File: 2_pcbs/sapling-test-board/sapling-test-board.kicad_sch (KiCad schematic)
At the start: 24 parts, among them IC1 LED driver TLC59281DBQR, IC2 LED driver TLC59281DBQR, IC3 74HC138D, J1 Pin header BCS-112-L-D-PE, J2 UJC-HP-3-SMT-TR

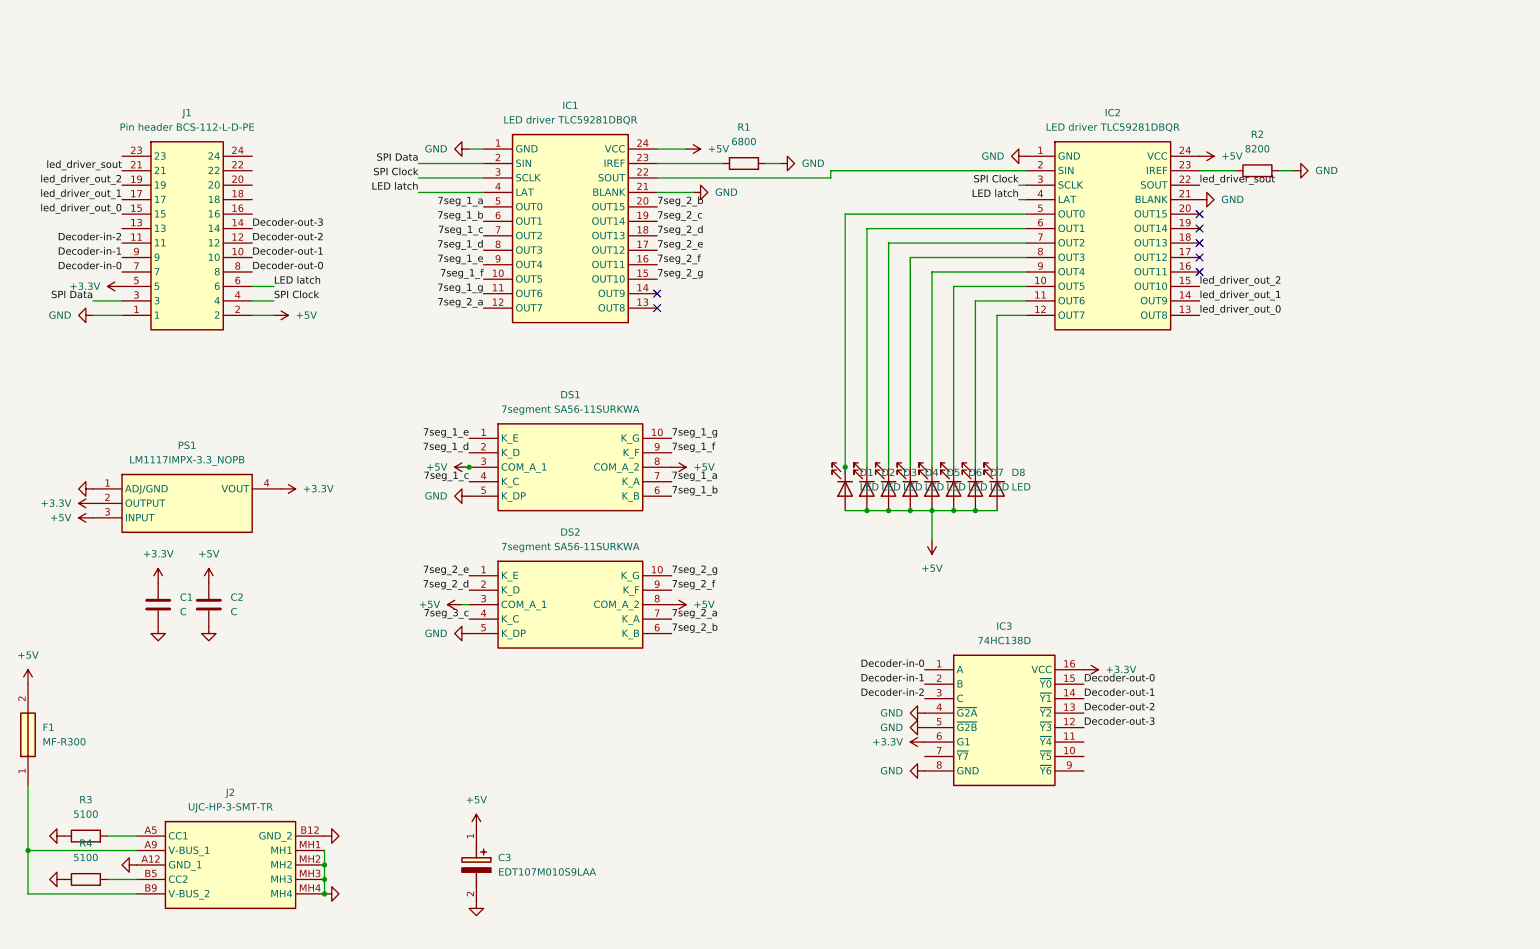
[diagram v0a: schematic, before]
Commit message: Hand routed PCB
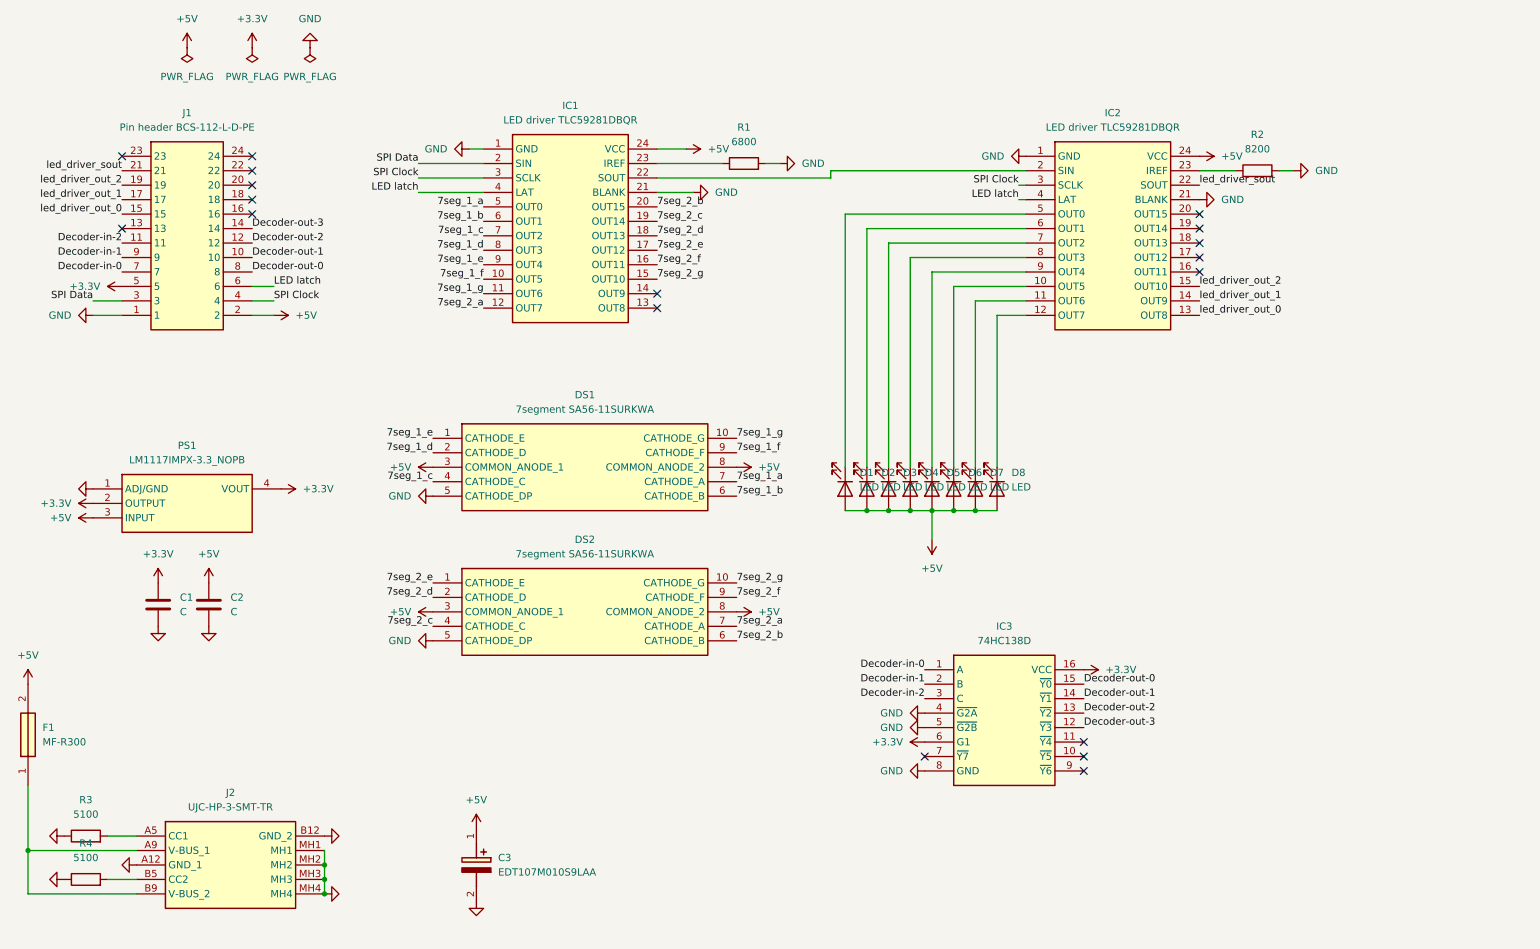
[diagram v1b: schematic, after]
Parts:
- C1, C2: footprint (none) -> Capacitor_SMD:C_0805_2012Metric
- C3: footprint CAPAE830X650N -> 100uf 10v Electrolytic cap:CAPAE830X650N
- D1, D2, D3, D4, D5, D6, D7, D8: footprint (none) -> LED_THT:LED_D5.0mm
- DS1, DS2: footprint DIPS1524W75P254L1270H825Q10N -> 7-segment:DIPS1524W75P254L1270H825Q10N; symbol 7-segment:SA56-11SURKWA -> 7-segment:SA56-11CGKWA; Manufacturer_Part_Number SA56-11SURKWA -> SA56-11CGKWA; Mouser Part Number 604-SA56-11SURKWA -> 604-SA56-11CGKWA; Mouser Price/Stock https://www.mouser.co.uk/ProductDetail/Kingbright/SA56-11SU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 -> https://www.mouser.co.uk/ProductDetail/Kingbright/SA56-11CG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
- F1: footprint MFR300 -> Resettable fuse:MFR300
- IC1, IC2: footprint SOP64P600X175-24N -> LED driver:SOP64P600X175-24N
- IC3: footprint SOIC127P600X175-16N -> 3-8 decoder:SOIC127P600X175-16N
- J1: footprint BCS-112-XXX-D-PE -> Pin header:BCS-112-XXX-D-PE
- J2: footprint UJCHP3SMTTR -> USB-C plug:UJCHP3SMTTR
- PS1: footprint SOT230P700X180-4N -> 3.3v regulator:SOT230P700X180-4N
- R1, R2, R3, R4: footprint (none) -> Resistor_SMD:R_0805_2012Metric
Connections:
- net 7seg_3_c is gone; now on net 7seg_2_c: DS2.4 (CATHODE_C)
- no-connect marks 7 -> 18
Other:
- moved on the sheet: DS1, DS2

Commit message: BB PCB review
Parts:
- added C4, C5, C6: 100nf, Capacitor_SMD:C_0805_2012Metric, symbol Device:C
- added TP1: LED Driver 2 sout, TestPoint:TestPoint_Pad_D4.0mm, symbol Connector:TestPoint
- added TP2: +5v, TestPoint:TestPoint_Pad_D4.0mm, symbol Connector:TestPoint
- added TP3: GND, TestPoint:TestPoint_Pad_D4.0mm, symbol Connector:TestPoint
- added TP4: +3.3v, TestPoint:TestPoint_Pad_D4.0mm, symbol Connector:TestPoint
- added TP5: SIN between, TestPoint:TestPoint_Pad_D4.0mm, symbol Connector:TestPoint
- C1, C2: value C -> 500nf
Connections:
- net +3.3V: now also C4.2, TP4.1
- net +5V: now also C5.2, C6.2, TP2.1
- net GND: now also C4.1, C5.1, C6.1, TP3.1
- net led_driver_sout: now also TP1.1
- net at IC1.22 (SOUT), IC2.2 (SIN): now also TP5.1

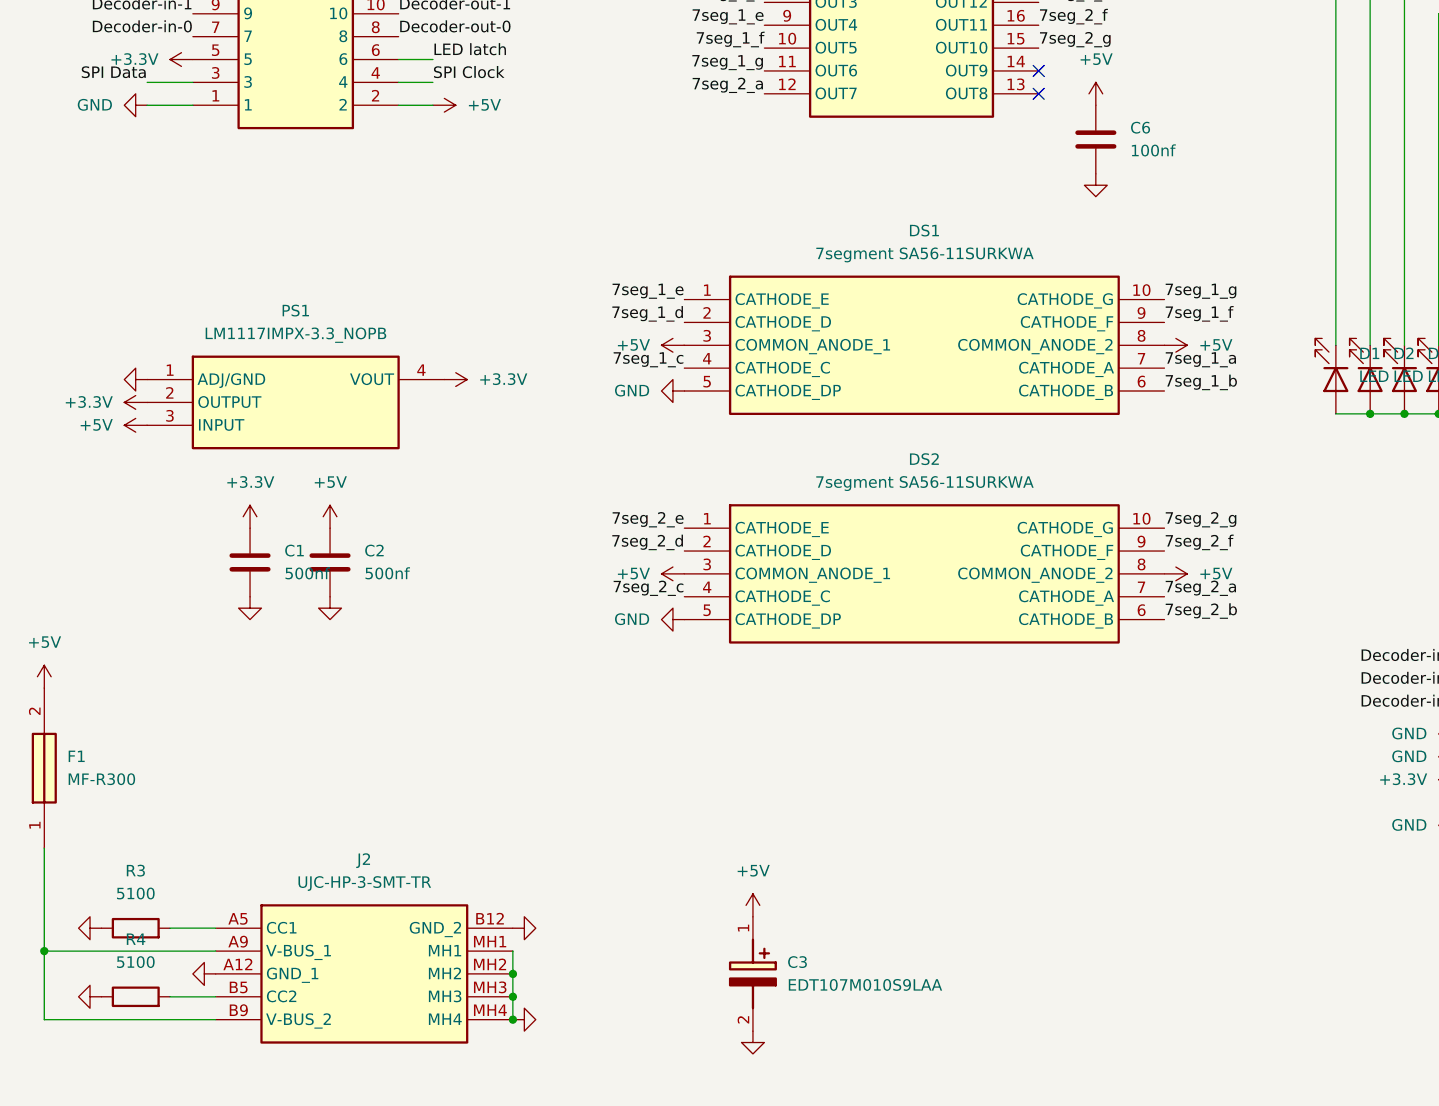
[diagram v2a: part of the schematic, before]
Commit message: Test board PCB ordered
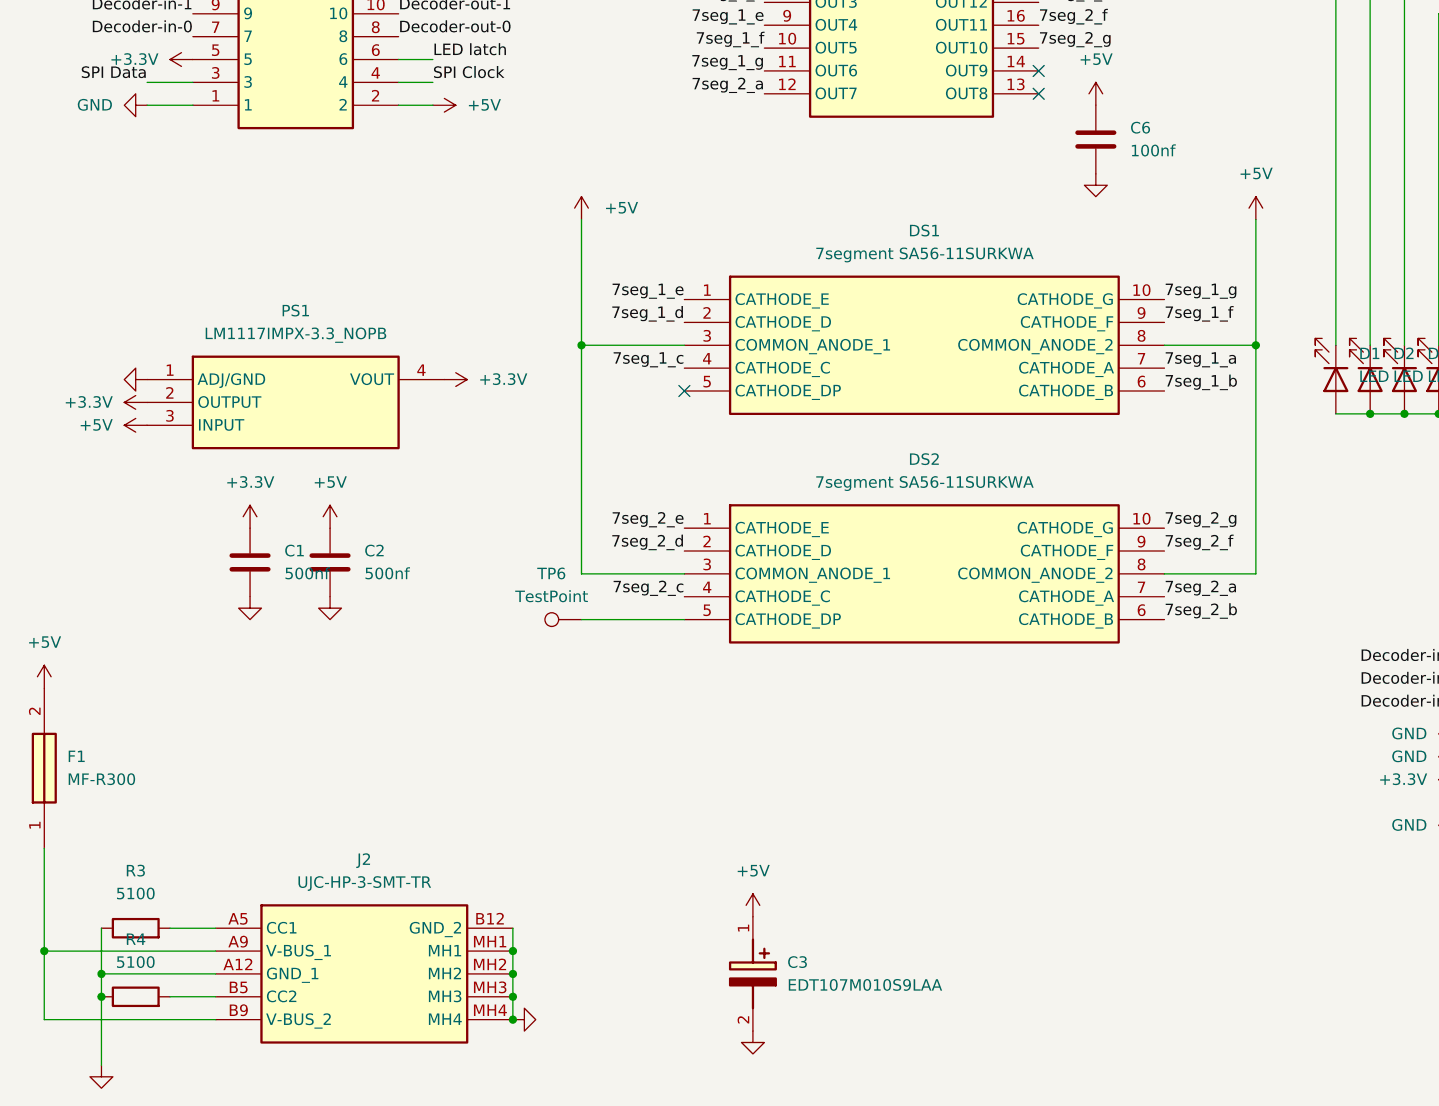
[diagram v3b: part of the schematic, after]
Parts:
- added TP6: TestPoint, TestPoint:TestPoint_Pad_D4.0mm, symbol Connector:TestPoint
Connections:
- net GND: no longer DS1.5 (CATHODE_DP), DS2.5 (CATHODE_DP)
- new net: DS2.5 (CATHODE_DP), TP6.1
- no-connect marks 18 -> 19
